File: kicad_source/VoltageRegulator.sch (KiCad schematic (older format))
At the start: 15 parts, among them U9 IFX91041EFJ

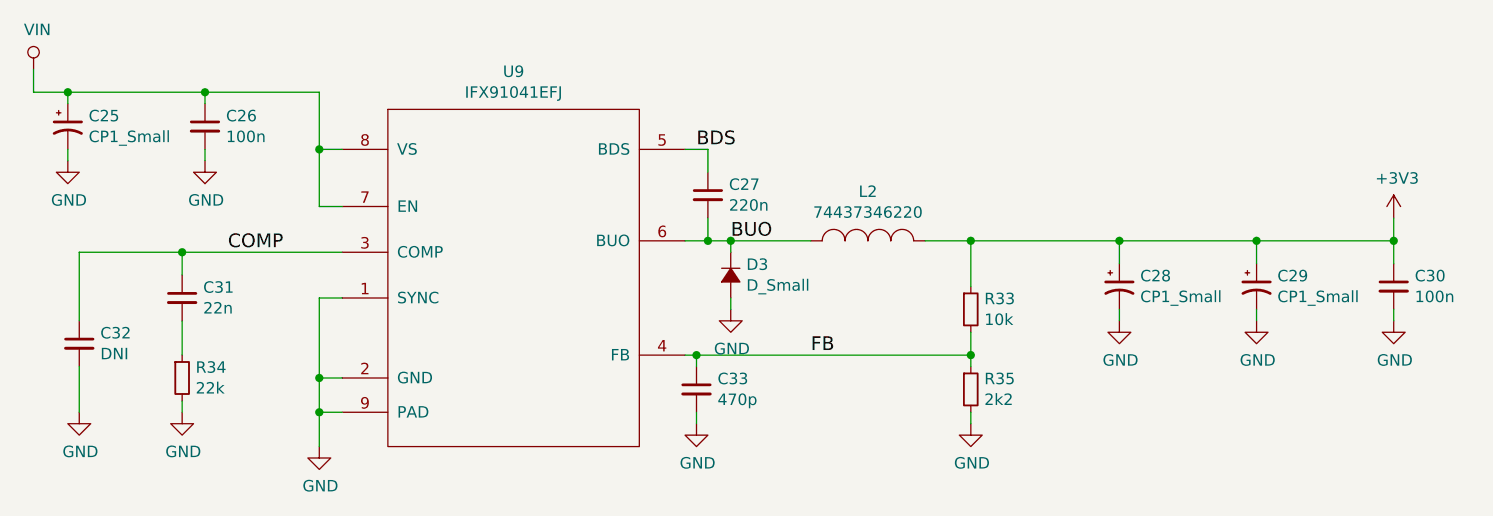
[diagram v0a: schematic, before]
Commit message: added values in schematic, generated pdf schematic
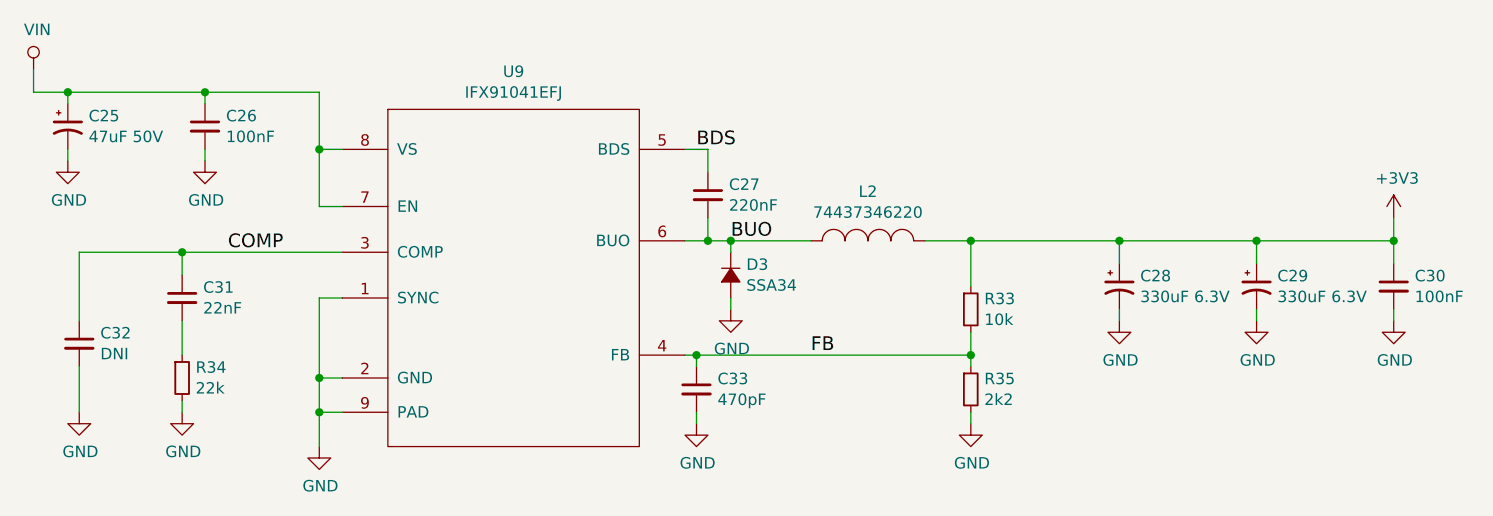
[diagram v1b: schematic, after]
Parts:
- C25: value CP1_Small -> 47uF 50V
- C26, C30: value 100n -> 100nF
- C27: value 220n -> 220nF
- C28, C29: value CP1_Small -> 330uF 6.3V
- C31: value 22n -> 22nF
- C33: value 470p -> 470pF
- D3: value D_Small -> SSA34
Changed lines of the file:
@@
 EESchema Schematic File Version 4
-LIBS:HighPowerMotorFeatherWing-cache
-EELAYER 26 0
+EELAYER 30 0
 EELAYER END
 $Descr A4 11693 8268
@@
 Sheet 4 5
 Title ""
-Date ""
+Date "2019-12-29"
 Rev ""
 Comp ""
@@
 P 3700 4000
 F 0 "C31" H 3792 4046 50  0000 L CNN
-F 1 "22n" H 3792 3955 50  0000 L CNN
+F 1 "22nF" H 3792 3955 50  0000 L CNN
 F 2 "capacitors:C_0603" H 3700 3850 50  0001 C CNN
 F 3 "" H 3700 4000 50  0000 C CNN
@@
 P 3800 3250
 F 0 "C26" H 3892 3296 50  0000 L CNN
-F 1 "100n" H 3892 3205 50  0000 L CNN
+F 1 "100nF" H 3892 3205 50  0000 L CNN
 F 2 "capacitors:C_0603" H 3800 3100 50  0001 C CNN
 F 3 "" H 3800 3250 50  0000 C CNN
@@
 P 5950 4400
 F 0 "C33" H 6042 4446 50  0000 L CNN
-F 1 "470p" H 6042 4355 50  0000 L CNN
+F 1 "470pF" H 6042 4355 50  0000 L CNN
 F 2 "capacitors:C_0603" H 5950 4250 50  0001 C CNN
 F 3 "" H 5950 4400 50  0000 C CNN
@@
 P 6000 3550
 F 0 "C27" H 6092 3596 50  0000 L CNN
-F 1 "220n" H 6092 3505 50  0000 L CNN
+F 1 "220nF" H 6092 3505 50  0000 L CNN
 F 2 "capacitors:C_0603" H 6000 3400 50  0001 C CNN
 F 3 "" H 6000 3550 50  0000 C CNN
@@
 P 7800 3950
 F 0 "C28" H 7891 3996 50  0000 L CNN
-F 1 "CP1_Small" H 7891 3905 50  0000 L CNN
+F 1 "330uF 6.3V" H 7891 3905 50  0000 L CNN
 F 2 "capacitors:TantalC_SizeD_EIA-7343_Wave" H 7900 3750 50  0001 C CNN
 F 3 "" H 7800 3950 50  0000 C CNN
@@
 P 8400 3950
 F 0 "C29" H 8491 3996 50  0000 L CNN
-F 1 "CP1_Small" H 8491 3905 50  0000 L CNN
+F 1 "330uF 6.3V" H 8491 3905 50  0000 L CNN
 F 2 "capacitors:TantalC_SizeD_EIA-7343_Wave" H 8500 3750 50  0001 C CNN
 F 3 "" H 8400 3950 50  0000 C CNN
@@
 P 3200 3250
 F 0 "C25" H 3291 3296 50  0000 L CNN
-F 1 "CP1_Small" H 3291 3205 50  0000 L CNN
+F 1 "47uF 50V" H 3291 3205 50  0000 L CNN
 F 2 "capacitors:TantalC_SizeD_EIA-7343_Wave" H 3300 3050 50  0001 C CNN
 F 3 "" H 3200 3250 50  0000 C CNN
@@
 P 9000 3950
 F 0 "C30" H 9092 3996 50  0000 L CNN
-F 1 "100n" H 9092 3905 50  0000 L CNN
+F 1 "100nF" H 9092 3905 50  0000 L CNN
 F 2 "capacitors:C_0603" H 9000 3800 50  0001 C CNN
 F 3 "" H 9000 3950 50  0000 C CNN
@@
 P 6100 3900
 F 0 "D3" V 6054 3968 50  0000 L CNN
-F 1 "D_Small" V 6145 3968 50  0000 L CNN
+F 1 "SSA34" V 6145 3968 50  0000 L CNN
 F 2 "diodes:SMA_Standard" V 6100 3900 50  0001 C CNN
 F 3 "" V 6100 3900 50  0000 C CNN

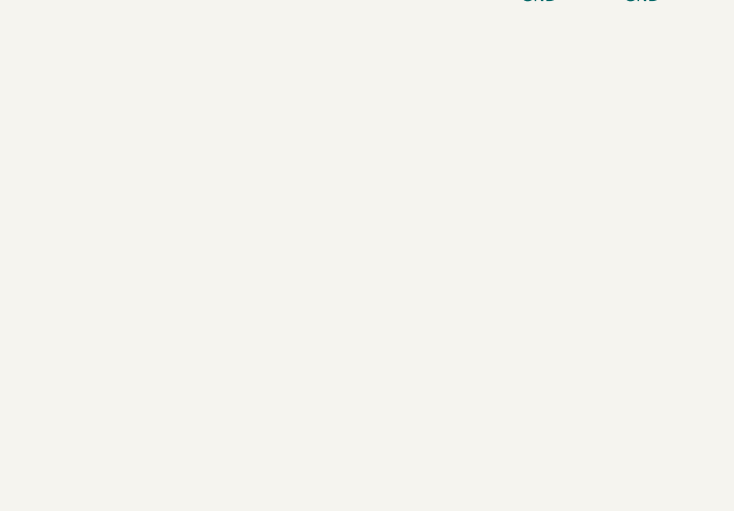
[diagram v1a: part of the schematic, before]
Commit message: changed mounting holes to parts and generated step file
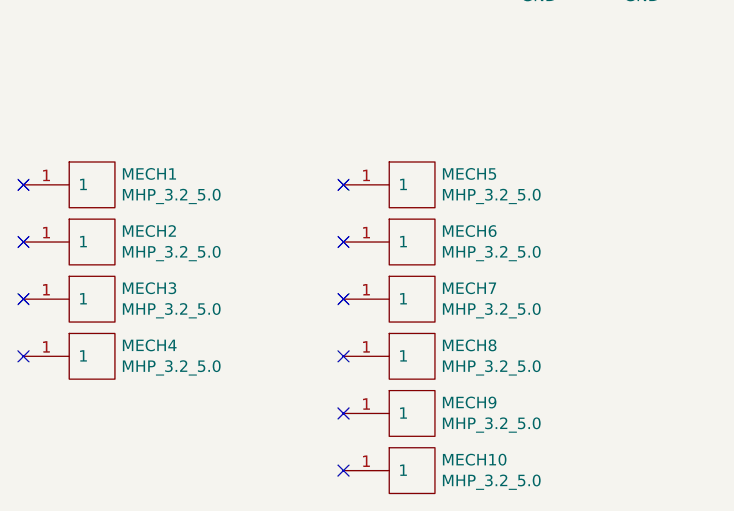
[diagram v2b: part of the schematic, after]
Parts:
- added MECH1, MECH10, MECH2, MECH3, MECH4, MECH5, MECH6, MECH7, MECH8, MECH9: MHP_3.2_5.0, MECH_mounting_holes:MHP_3.2_5.0, symbol MECH_mounting-holes:MHP_3.2_5.0
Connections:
- no-connect marks 0 -> 10
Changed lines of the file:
@@
 Wire Wire Line
 	6100 3750 6450 3750
+$Comp
+L MECH_mounting-holes:MHP_3.2_5.0 MECH1
+U 1 1 5E993D4D
+P 1300 5500
+F 0 "MECH1" H 1428 5546 50  0000 L CNN
+F 1 "MHP_3.2_5.0" H 1428 5455 50  0000 L CNN
+F 2 "MECH_mounting_holes:MHP_3.2_5.0" H 1200 5550 50  0001 C CNN
+F 3 "" H 1300 5500 50  0001 C CNN
+	1    1300 5500
+	1    0    0    -1
+$EndComp
+$Comp
+L MECH_mounting-holes:MHP_3.2_5.0 MECH2
+U 1 1 5E9943C9
+P 1300 5750
+F 0 "MECH2" H 1428 5796 50  0000 L CNN
+F 1 "MHP_3.2_5.0" H 1428 5705 50  0000 L CNN
+F 2 "MECH_mounting_holes:MHP_3.2_5.0" H 1200 5800 50  0001 C CNN
+F 3 "" H 1300 5750 50  0001 C CNN
+	1    1300 5750
+	1    0    0    -1
+$EndComp
+$Comp
+L MECH_mounting-holes:MHP_3.2_5.0 MECH3
+U 1 1 5E994577
+P 1300 6000
+F 0 "MECH3" H 1428 6046 50  0000 L CNN
+F 1 "MHP_3.2_5.0" H 1428 5955 50  0000 L CNN
+F 2 "MECH_mounting_holes:MHP_3.2_5.0" H 1200 6050 50  0001 C CNN
+F 3 "" H 1300 6000 50  0001 C CNN
+	1    1300 6000
+	1    0    0    -1
+$EndComp
+$Comp
+L MECH_mounting-holes:MHP_3.2_5.0 MECH4
+U 1 1 5E9947A1
+P 1300 6250
+F 0 "MECH4" H 1428 6296 50  0000 L CNN
+F 1 "MHP_3.2_5.0" H 1428 6205 50  0000 L CNN
+F 2 "MECH_mounting_holes:MHP_3.2_5.0" H 1200 6300 50  0001 C CNN
+F 3 "" H 1300 6250 50  0001 C CNN
+	1    1300 6250
+	1    0    0    -1
+$EndComp
+NoConn ~ 1000 5500
+NoConn ~ 1000 5750
+NoConn ~ 1000 6000
+NoConn ~ 1000 6250
+$Comp
+L MECH_mounting-holes:MHP_3.2_5.0 MECH5
+U 1 1 5E99A7D8
+P 2700 5500
+F 0 "MECH5" H 2828 5546 50  0000 L CNN
+F 1 "MHP_3.2_5.0" H 2828 5455 50  0000 L CNN
+F 2 "MECH_mounting_holes:MHP_3.2_5.0" H 2600 5550 50  0001 C CNN
+F 3 "" H 2700 5500 50  0001 C CNN
+	1    2700 5500
+	1    0    0    -1
+$EndComp
+$Comp
+L MECH_mounting-holes:MHP_3.2_5.0 MECH6
+U 1 1 5E99A7E2
+P 2700 5750
+F 0 "MECH6" H 2828 5796 50  0000 L CNN
+F 1 "MHP_3.2_5.0" H 2828 5705 50  0000 L CNN
+F 2 "MECH_mounting_holes:MHP_3.2_5.0" H 2600 5800 50  0001 C CNN
+F 3 "" H 2700 5750 50  0001 C CNN
+	1    2700 5750
+	1    0    0    -1
+$EndComp
+$Comp
+L MECH_mounting-holes:MHP_3.2_5.0 MECH7
+U 1 1 5E99A7EC
+P 2700 6000
+F 0 "MECH7" H 2828 6046 50  0000 L CNN
+F 1 "MHP_3.2_5.0" H 2828 5955 50  0000 L CNN
+F 2 "MECH_mounting_holes:MHP_3.2_5.0" H 2600 6050 50  0001 C CNN
+F 3 "" H 2700 6000 50  0001 C CNN
+	1    2700 6000
+	1    0    0    -1
+$EndComp
+$Comp
+L MECH_mounting-holes:MHP_3.2_5.0 MECH8
+U 1 1 5E99A7F6
+P 2700 6250
+F 0 "MECH8" H 2828 6296 50  0000 L CNN
+F 1 "MHP_3.2_5.0" H 2828 6205 50  0000 L CNN
+F 2 "MECH_mounting_holes:MHP_3.2_5.0" H 2600 6300 50  0001 C CNN
+F 3 "" H 2700 6250 50  0001 C CNN
+	1    2700 6250
+	1    0    0    -1
+$EndComp
+NoConn ~ 2400 5500
+NoConn ~ 2400 5750
+NoConn ~ 2400 6000
+NoConn ~ 2400 6250
+$Comp
+L MECH_mounting-holes:MHP_3.2_5.0 MECH9
+U 1 1 5E99D39B
+P 2700 6500
+F 0 "MECH9" H 2828 6546 50  0000 L CNN
+F 1 "MHP_3.2_5.0" H 2828 6455 50  0000 L CNN
+F 2 "MECH_mounting_holes:MHP_3.2_5.0" H 2600 6550 50  0001 C CNN
+F 3 "" H 2700 6500 50  0001 C CNN
+	1    2700 6500
+	1    0    0    -1
+$EndComp
+$Comp
+L MECH_mounting-holes:MHP_3.2_5.0 MECH10
+U 1 1 5E99D3A5
+P 2700 6750
+F 0 "MECH10" H 2828 6796 50  0000 L CNN
+F 1 "MHP_3.2_5.0" H 2828 6705 50  0000 L CNN
+F 2 "MECH_mounting_holes:MHP_3.2_5.0" H 2600 6800 50  0001 C CNN
+F 3 "" H 2700 6750 50  0001 C CNN
+	1    2700 6750
+	1    0    0    -1
+$EndComp
+NoConn ~ 2400 6500
+NoConn ~ 2400 6750
 $EndSCHEMATC
